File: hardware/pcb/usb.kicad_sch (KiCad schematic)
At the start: 6 parts, among them J3 USB_C_Receptacle_USB2.0_16P, U5 ECMF02-2AMX6

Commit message: started cleaning up schematic
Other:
- company: (none) -> Gensis
- title: (none) -> USB
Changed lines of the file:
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@@
 	(generator_version "10.0")
 	(paper "A5")
+	(title_block
+		(title "USB")
+		(rev "v1.0.0")
+		(company "Gensis")
+	)
 	(rectangle
 		(start 138.43 33.02)

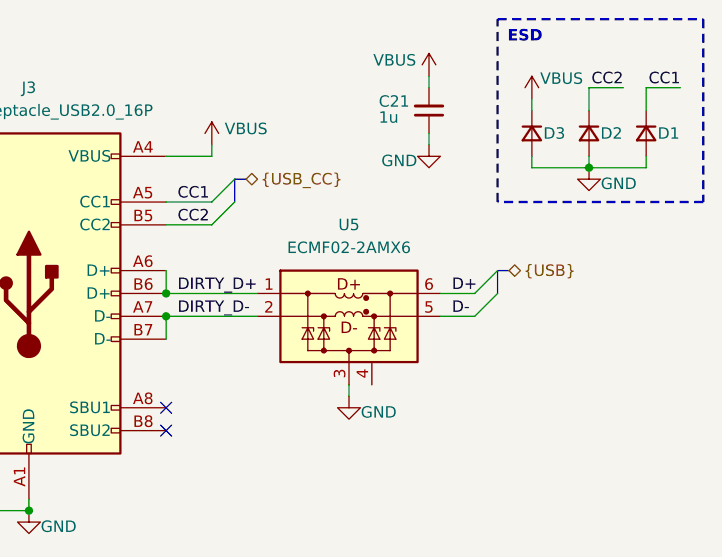
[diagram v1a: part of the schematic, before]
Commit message: main board: fixed schematic errors, made sama7 symbol better
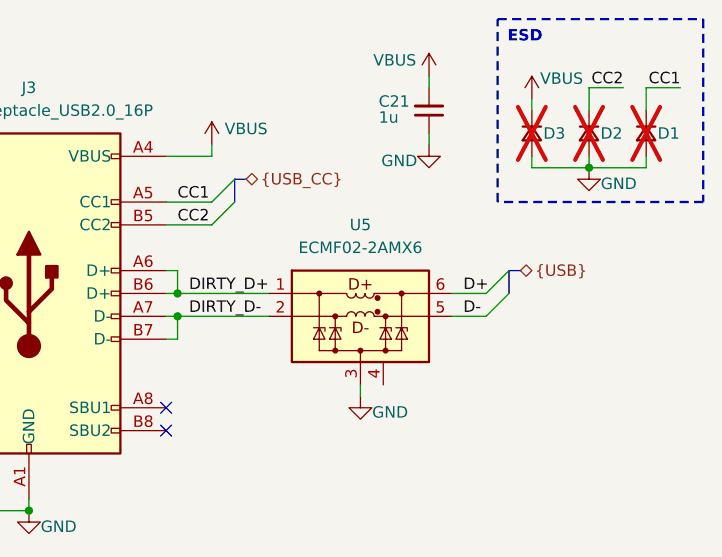
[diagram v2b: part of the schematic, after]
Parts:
- D1, D2, D3: now not fitted; now left out of the parts list
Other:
- moved on the sheet: U5
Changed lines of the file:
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@@
 	)
 	(junction
-		(at 101.6 66.04)
+		(at 102.87 66.04)
 		(diameter 0)
 		(color 0 0 0 0)
@@
 	)
 	(junction
-		(at 101.6 63.5)
+		(at 102.87 63.5)
 		(diameter 0)
 		(color 0 0 0 0)
@@
 	)
 	(bus_entry
-		(at 138.43 63.5)
+		(at 139.7 63.5)
 		(size -2.54 2.54)
 		(stroke
@@
 	)
 	(bus_entry
-		(at 138.43 60.96)
+		(at 139.7 60.96)
 		(size -2.54 2.54)
 		(stroke
@@
 	(wire
 		(pts
-			(xy 121.92 73.66) (xy 121.92 74.93)
-		)
-		(stroke
-			(width 0)
-			(type default)
-		)
-	)
-	(wire
-		(pts
-			(xy 101.6 66.04) (xy 111.76 66.04)
+			(xy 123.19 73.66) (xy 123.19 74.93)
 		)
 		(stroke
@@
 	(wire
 		(pts
+			(xy 102.87 60.96) (xy 101.6 60.96)
+		)
+		(stroke
+			(width 0)
+			(type default)
+		)
+	)
+	(wire
+		(pts
 			(xy 154.94 40.64) (xy 158.75 40.64)
 		)
@@
 	(wire
 		(pts
+			(xy 102.87 63.5) (xy 101.6 63.5)
+		)
+		(stroke
+			(width 0)
+			(type default)
+		)
+	)
+	(wire
+		(pts
 			(xy 142.24 48.26) (xy 142.24 49.53)
 		)
@@
 		)
 	)
+	(wire
+		(pts
+			(xy 102.87 66.04) (xy 113.03 66.04)
+		)
+		(stroke
+			(width 0)
+			(type default)
+		)
+	)
 	(bus
 		(pts
-			(xy 138.43 60.96) (xy 138.43 63.5)
+			(xy 139.7 60.96) (xy 139.7 63.5)
 		)
 		(stroke
@@
 	(wire
 		(pts
+			(xy 102.87 66.04) (xy 101.6 66.04)
+		)
+		(stroke
+			(width 0)
+			(type default)
+		)
+	)
+	(wire
+		(pts
+			(xy 102.87 68.58) (xy 101.6 68.58)
+		)
+		(stroke
+			(width 0)
+			(type default)
+		)
+	)
+	(wire
+		(pts
 			(xy 148.59 48.26) (xy 148.59 49.53)
 		)
@@
 	(wire
 		(pts
-			(xy 132.08 66.04) (xy 135.89 66.04)
+			(xy 133.35 66.04) (xy 137.16 66.04)
 		)
 		(stroke
@@
 	(wire
 		(pts
-			(xy 132.08 63.5) (xy 135.89 63.5)
+			(xy 133.35 63.5) (xy 137.16 63.5)
 		)
 		(stroke
@@
 	(wire
 		(pts
-			(xy 101.6 63.5) (xy 111.76 63.5)
-		)
-		(stroke
-			(width 0)
-			(type default)
-		)
-	)
-	(wire
-		(pts
 			(xy 101.6 55.88) (xy 106.68 55.88)
 		)
@@
 	(wire
 		(pts
-			(xy 101.6 66.04) (xy 101.6 68.58)
+			(xy 102.87 66.04) (xy 102.87 68.58)
+		)
+		(stroke
+			(width 0)
+			(type default)
+		)
+	)
+	(wire
+		(pts
+			(xy 102.87 63.5) (xy 113.03 63.5)
 		)
 		(stroke
@@
 	(bus
 		(pts
-			(xy 139.7 60.96) (xy 138.43 60.96)
-		)
-		(stroke
-			(width 0)
-			(type default)
-		)
-	)
-	(wire
-		(pts
-			(xy 101.6 60.96) (xy 101.6 63.5)
+			(xy 140.97 60.96) (xy 139.7 60.96)
+		)
+		(stroke
+			(width 0)
+			(type default)
+		)
+	)
+	(wire
+		(pts
+			(xy 102.87 60.96) (xy 102.87 63.5)
 		)
 		(stroke
@@
 	)
 	(label "DIRTY_D+"
-		(at 102.87 63.5 0)
+		(at 104.14 63.5 0)
 		(effects
 			(font
@@
 	)
 	(label "DIRTY_D-"
-		(at 102.87 66.04 0)
+		(at 104.14 66.04 0)
 		(effects
 			(font
@@
 	)
 	(label "D+"
-		(at 133.35 63.5 0)
+		(at 134.62 63.5 0)
 		(effects
 			(font
@@
 	)
 	(label "D-"
-		(at 133.35 66.04 0)
+		(at 134.62 66.04 0)
 		(effects
 			(font
@@
 	(hierarchical_label "{USB}"
 		(shape bidirectional)
-		(at 139.7 60.96 0)
+		(at 140.97 60.96 0)
 		(effects
 			(font
@@
 		(body_style 1)
 		(exclude_from_sim no)
-		(in_bom yes)
-		(on_board yes)
-		(in_pos_files yes)
-		(dnp no)
+		(in_bom no)
+		(on_board no)
+		(in_pos_files no)
+		(dnp yes)
 		(property "Reference" "D1"
 			(at 156.21 45.72 90)
@@
 	(symbol
 		(lib_id "Power_Protection:ECMF02-2AMX6")
-		(at 121.92 66.04 0)
+		(at 123.19 66.04 0)
 		(unit 1)
 		(body_style 1)
@@
 		(fields_autoplaced yes)
 		(property "Reference" "U5"
-			(at 121.92 55.88 0)
+			(at 123.19 55.88 0)
 			(show_name no)
 			(do_not_autoplace no)
@@
 		)
 		(property "Value" "ECMF02-2AMX6"
-			(at 121.92 58.42 0)
+			(at 123.19 58.42 0)
 			(show_name no)
 			(do_not_autoplace no)
@@
 		)
 		(property "Footprint" "Package_DFN_QFN:ST_UQFN-6L_1.5x1.7mm_P0.5mm"
-			(at 121.92 86.36 0)
+			(at 123.19 86.36 0)
 			(hide yes)
 			(show_name no)
@@
 		)
 		(property "Datasheet" "https://www.st.com/resource/en/datasheet/ecmf02-2amx6.pdf"
-			(at 121.92 88.9 0)
+			(at 123.19 88.9 0)
 			(hide yes)
 			(show_name no)
@@
 		)
 		(property "Description" "Single Pair Common Mode Filter with ESD Protection, UQFN-6L"
-			(at 121.92 66.04 0)
+			(at 123.19 66.04 0)
 			(hide yes)
 			(show_name no)
@@
 		)
 		(property "KLC_S3.3" ""
-			(at 121.92 66.04 0)
+			(at 123.19 66.04 0)
 			(hide yes)
 			(show_name no)
@@
 		)
 		(property "KLC_S4.1" ""
-			(at 121.92 66.04 0)
+			(at 123.19 66.04 0)
 			(hide yes)
 			(show_name no)
@@
 	(symbol
 		(lib_id "power:GND")
-		(at 121.92 74.93 0)
+		(at 123.19 74.93 0)
 		(unit 1)
 		(body_style 1)
@@
 		(dnp no)
 		(property "Reference" "#PWR013"
-			(at 121.92 81.28 0)
+			(at 123.19 81.28 0)
 			(hide yes)
 			(show_name no)
@@
 		)
 		(property "Value" "GND"
-			(at 125.222 76.708 0)
+			(at 126.492 76.708 0)
 			(show_name no)
 			(do_not_autoplace no)
@@
 		)
 		(property "Footprint" ""
-			(at 121.92 74.93 0)
+			(at 123.19 74.93 0)
 			(hide yes)
 			(show_name no)
@@
 		)
 		(property "Datasheet" ""
-			(at 121.92 74.93 0)
+			(at 123.19 74.93 0)
 			(hide yes)
 			(show_name no)
@@
 		)
 		(property "Description" "Power symbol creates a global label with name \"GND\" , ground"
-			(at 121.92 74.93 0)
+			(at 123.19 74.93 0)
 			(hide yes)
 			(show_name no)
@@
 		(body_style 1)
 		(exclude_from_sim no)
-		(in_bom yes)
-		(on_board yes)
-		(in_pos_files yes)
-		(dnp no)
+		(in_bom no)
+		(on_board no)
+		(in_pos_files no)
+		(dnp yes)
 		(property "Reference" "D3"
 			(at 143.51 45.72 90)
@@
 		(body_style 1)
 		(exclude_from_sim no)
-		(in_bom yes)
-		(on_board yes)
-		(in_pos_files yes)
-		(dnp no)
+		(in_bom no)
+		(on_board no)
+		(in_pos_files no)
+		(dnp yes)
 		(property "Reference" "D2"
 			(at 149.86 45.72 90)

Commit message: mainboard: adde notes
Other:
- note added: "No ESD protection added for these nets For first protype this is fine Will be added later"
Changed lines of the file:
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@@
+		)
+	)
+	(text "No ESD protection added for these nets\nFor first protype this is fine\nWill be added later"
+		(exclude_from_sim no)
+		(at 138.684 32.512 0)
+		(effects
+			(font
+				(size 1.27 1.27)
+				(thickness 0.1588)
+			)
+			(justify left bottom)
 		)
 	)

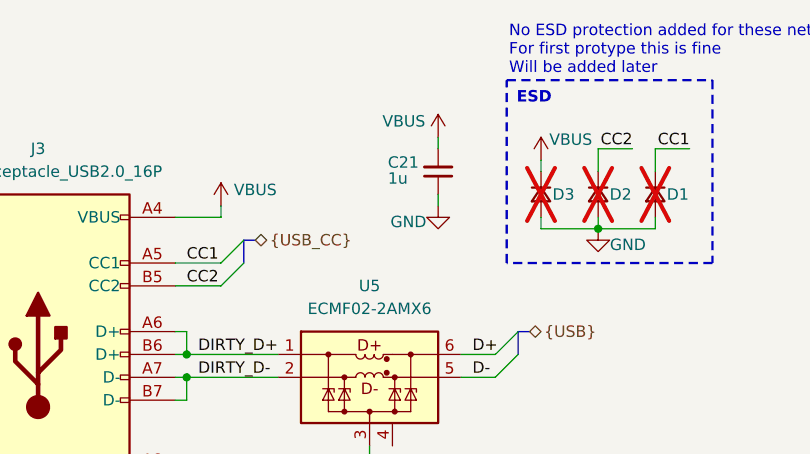
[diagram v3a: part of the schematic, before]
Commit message: mainboard: finished touchpad schematic
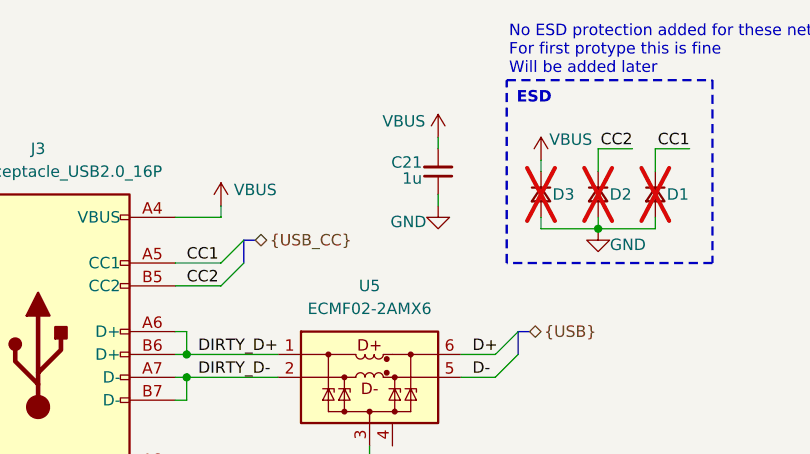
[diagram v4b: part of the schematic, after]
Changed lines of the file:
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@@
 		(dnp no)
 		(property "Reference" "C21"
-			(at 125.222 42.164 0)
+			(at 129.032 42.164 0)
 			(show_name no)
 			(do_not_autoplace no)
@@
 					(size 1.27 1.27)
 				)
-				(justify left)
+				(justify right)
 			)
 		)
 		(property "Value" "1u"
-			(at 125.222 43.942 0)
+			(at 129.032 43.942 0)
 			(show_name no)
 			(do_not_autoplace no)
@@
 					(size 1.27 1.27)
 				)
-				(justify left)
+				(justify right)
 			)
 		)

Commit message: mainboard: reannotated schematic
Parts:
- renumbered C21 to C110, D3 to D2, D2 to D3, D1 to D4, U5 to U6
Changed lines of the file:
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@@
 		(in_pos_files yes)
 		(dnp no)
-		(property "Reference" "#PWR012"
+		(property "Reference" "#PWR0102"
 			(at 86.36 93.98 0)
 			(hide yes)
@@
 			(project "meko"
 				(path "/da54f10a-146b-4941-a9c7-55c7173bb101/13ed9585-0f16-442f-add9-c716aca8a0ac"
-					(reference "#PWR012")
+					(reference "#PWR0102")
 					(unit 1)
 				)
@@
 		(in_pos_files no)
 		(dnp yes)
-		(property "Reference" "D1"
+		(property "Reference" "D4"
 			(at 156.21 45.72 90)
 			(show_name no)
@@
 			(project "meko"
 				(path "/da54f10a-146b-4941-a9c7-55c7173bb101/13ed9585-0f16-442f-add9-c716aca8a0ac"
-					(reference "D1")
+					(reference "D4")
 					(unit 1)
 				)
@@
 		(dnp no)
 		(fields_autoplaced yes)
-		(property "Reference" "U5"
+		(property "Reference" "U6"
 			(at 123.19 55.88 0)
 			(show_name no)
@@
 			(project "meko"
 				(path "/da54f10a-146b-4941-a9c7-55c7173bb101/13ed9585-0f16-442f-add9-c716aca8a0ac"
-					(reference "U5")
+					(reference "U6")
 					(unit 1)
 				)
@@
 		(in_pos_files yes)
 		(dnp no)
-		(property "Reference" "#PWR013"
+		(property "Reference" "#PWR0101"
 			(at 123.19 81.28 0)
 			(hide yes)
@@
 			(project "meko"
 				(path "/da54f10a-146b-4941-a9c7-55c7173bb101/13ed9585-0f16-442f-add9-c716aca8a0ac"
-					(reference "#PWR013")
+					(reference "#PWR0101")
 					(unit 1)
 				)
@@
 		(in_pos_files yes)
 		(dnp no)
-		(property "Reference" "#PWR019"
+		(property "Reference" "#PWR099"
 			(at 130.81 53.34 0)
 			(hide yes)
@@
 			(project "meko"
 				(path "/da54f10a-146b-4941-a9c7-55c7173bb101/13ed9585-0f16-442f-add9-c716aca8a0ac"
-					(reference "#PWR019")
+					(reference "#PWR099")
 					(unit 1)
 				)
@@
 		(in_pos_files yes)
 		(dnp no)
-		(property "Reference" "#PWR015"
+		(property "Reference" "#PWR097"
 			(at 142.24 45.72 0)
 			(hide yes)
@@
 			(project "meko"
 				(path "/da54f10a-146b-4941-a9c7-55c7173bb101/13ed9585-0f16-442f-add9-c716aca8a0ac"
-					(reference "#PWR015")
+					(reference "#PWR097")
 					(unit 1)
 				)
@@
 		(in_pos_files yes)
 		(dnp no)
-		(property "Reference" "#PWR016"
+		(property "Reference" "#PWR0100"
 			(at 148.59 55.88 0)
 			(hide yes)
@@
 			(project "meko"
 				(path "/da54f10a-146b-4941-a9c7-55c7173bb101/13ed9585-0f16-442f-add9-c716aca8a0ac"
-					(reference "#PWR016")
+					(reference "#PWR0100")
 					(unit 1)
 				)
@@
 		(in_pos_files yes)
 		(dnp no)
-		(property "Reference" "#PWR014"
+		(property "Reference" "#PWR098"
 			(at 106.68 50.8 0)
 			(hide yes)
@@
 			(project "meko"
 				(path "/da54f10a-146b-4941-a9c7-55c7173bb101/13ed9585-0f16-442f-add9-c716aca8a0ac"
-					(reference "#PWR014")
+					(reference "#PWR098")
 					(unit 1)
 				)
@@
 		(in_pos_files yes)
 		(dnp no)
-		(property "Reference" "C21"
+		(property "Reference" "C110"
 			(at 129.032 42.164 0)
 			(show_name no)
@@
 			(project "meko"
 				(path "/da54f10a-146b-4941-a9c7-55c7173bb101/13ed9585-0f16-442f-add9-c716aca8a0ac"
-					(reference "C21")
+					(reference "C110")
 					(unit 1)
 				)
@@
 		(in_pos_files no)
 		(dnp yes)
-		(property "Reference" "D3"
+		(property "Reference" "D2"
 			(at 143.51 45.72 90)
 			(show_name no)
@@
 			(project "meko"
 				(path "/da54f10a-146b-4941-a9c7-55c7173bb101/13ed9585-0f16-442f-add9-c716aca8a0ac"
-					(reference "D3")
+					(reference "D2")
 					(unit 1)
 				)
@@
 		(in_pos_files no)
 		(dnp yes)
-		(property "Reference" "D2"
+		(property "Reference" "D3"
 			(at 149.86 45.72 90)
 			(show_name no)
@@
 			(project "meko"
 				(path "/da54f10a-146b-4941-a9c7-55c7173bb101/13ed9585-0f16-442f-add9-c716aca8a0ac"
-					(reference "D2")
+					(reference "D3")
 					(unit 1)
 				)
@@
 		(in_pos_files yes)
 		(dnp no)
-		(property "Reference" "#PWR018"
+		(property "Reference" "#PWR096"
 			(at 130.81 43.18 0)
 			(hide yes)
@@
 			(project "meko"
 				(path "/da54f10a-146b-4941-a9c7-55c7173bb101/13ed9585-0f16-442f-add9-c716aca8a0ac"
-					(reference "#PWR018")
+					(reference "#PWR096")
 					(unit 1)
 				)

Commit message: added a bunch testpoints
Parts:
- added TP20: CC1, TestPoint:TestPoint_Pad_D1.0mm, symbol Connector:TestPoint
- added TP21: CC2, TestPoint:TestPoint_Pad_D1.0mm, symbol Connector:TestPoint
- added TP51: VBUS, TestPoint:TestPoint_Pad_D1.0mm, symbol Connector:TestPoint
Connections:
- net CC1: now also TP20.1
- net CC2: now also TP21.1
- net VBUS: now also TP51.1
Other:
- moved on the sheet: C110, D2, D3, D4, J3, U6

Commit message: removed testpoints on sd cards, since I can probe the pins there
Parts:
- renumbered TP51 to TP47, TP20 to TP48, TP21 to TP49
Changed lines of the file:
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@@
 		(in_pos_files yes)
 		(dnp no)
-		(property "Reference" "#PWR0102"
+		(property "Reference" "#PWR096"
 			(at 36.83 93.98 0)
 			(hide yes)
@@
 			(project "meko"
 				(path "/da54f10a-146b-4941-a9c7-55c7173bb101/13ed9585-0f16-442f-add9-c716aca8a0ac"
-					(reference "#PWR0102")
+					(reference "#PWR096")
 					(unit 1)
 				)
@@
 		(in_pos_files yes)
 		(dnp no)
-		(property "Reference" "TP21"
+		(property "Reference" "TP49"
 			(at 141.224 81.026 90)
 			(show_name no)
@@
 			(project "meko"
 				(path "/da54f10a-146b-4941-a9c7-55c7173bb101/13ed9585-0f16-442f-add9-c716aca8a0ac"
-					(reference "TP21")
+					(reference "TP49")
 					(unit 1)
 				)
@@
 		(in_pos_files yes)
 		(dnp no)
-		(property "Reference" "TP51"
+		(property "Reference" "TP47"
 			(at 54.61 33.782 0)
 			(show_name no)
@@
 			(project "meko"
 				(path "/da54f10a-146b-4941-a9c7-55c7173bb101/13ed9585-0f16-442f-add9-c716aca8a0ac"
-					(reference "TP51")
+					(reference "TP47")
 					(unit 1)
 				)
@@
 		(in_pos_files yes)
 		(dnp no)
-		(property "Reference" "#PWR0101"
+		(property "Reference" "#PWR098"
 			(at 73.66 81.28 0)
 			(hide yes)
@@
 			(project "meko"
 				(path "/da54f10a-146b-4941-a9c7-55c7173bb101/13ed9585-0f16-442f-add9-c716aca8a0ac"
-					(reference "#PWR0101")
+					(reference "#PWR098")
 					(unit 1)
 				)
@@
 		(in_pos_files yes)
 		(dnp no)
-		(property "Reference" "#PWR099"
+		(property "Reference" "#PWR0100"
 			(at 81.28 53.34 0)
 			(hide yes)
@@
 			(project "meko"
 				(path "/da54f10a-146b-4941-a9c7-55c7173bb101/13ed9585-0f16-442f-add9-c716aca8a0ac"
-					(reference "#PWR099")
+					(reference "#PWR0100")
 					(unit 1)
 				)
@@
 		(in_pos_files yes)
 		(dnp no)
-		(property "Reference" "#PWR097"
+		(property "Reference" "#PWR0101"
 			(at 92.71 45.72 0)
 			(hide yes)
@@
 			(project "meko"
 				(path "/da54f10a-146b-4941-a9c7-55c7173bb101/13ed9585-0f16-442f-add9-c716aca8a0ac"
-					(reference "#PWR097")
+					(reference "#PWR0101")
 					(unit 1)
 				)
@@
 		(in_pos_files yes)
 		(dnp no)
-		(property "Reference" "#PWR0100"
+		(property "Reference" "#PWR0102"
 			(at 99.06 55.88 0)
 			(hide yes)
@@
 			(project "meko"
 				(path "/da54f10a-146b-4941-a9c7-55c7173bb101/13ed9585-0f16-442f-add9-c716aca8a0ac"
-					(reference "#PWR0100")
+					(reference "#PWR0102")
 					(unit 1)
 				)
@@
 		(in_pos_files yes)
 		(dnp no)
-		(property "Reference" "#PWR098"
+		(property "Reference" "#PWR097"
 			(at 57.15 50.8 0)
 			(hide yes)
@@
 			(project "meko"
 				(path "/da54f10a-146b-4941-a9c7-55c7173bb101/13ed9585-0f16-442f-add9-c716aca8a0ac"
-					(reference "#PWR098")
+					(reference "#PWR097")
 					(unit 1)
 				)
@@
 		(in_pos_files yes)
 		(dnp no)
-		(property "Reference" "TP20"
+		(property "Reference" "TP48"
 			(at 141.224 78.486 90)
 			(show_name no)
@@
 			(project "meko"
 				(path "/da54f10a-146b-4941-a9c7-55c7173bb101/13ed9585-0f16-442f-add9-c716aca8a0ac"
-					(reference "TP20")
+					(reference "TP48")
 					(unit 1)
 				)
@@
 		(in_pos_files yes)
 		(dnp no)
-		(property "Reference" "#PWR096"
+		(property "Reference" "#PWR099"
 			(at 81.28 43.18 0)
 			(hide yes)
@@
 			(project "meko"
 				(path "/da54f10a-146b-4941-a9c7-55c7173bb101/13ed9585-0f16-442f-add9-c716aca8a0ac"
-					(reference "#PWR096")
-					(unit 1)
-				)
+					(reference "#PWR099")
+					(unit 1)
+				)

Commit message: added capacitor to sama ddr vref pin
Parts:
- renumbered C110 to C112
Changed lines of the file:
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@@
 		(in_pos_files yes)
 		(dnp no)
-		(property "Reference" "#PWR096"
+		(property "Reference" "#PWR098"
 			(at 36.83 93.98 0)
 			(hide yes)
@@
 			(project "meko"
 				(path "/da54f10a-146b-4941-a9c7-55c7173bb101/13ed9585-0f16-442f-add9-c716aca8a0ac"
-					(reference "#PWR096")
+					(reference "#PWR098")
 					(unit 1)
 				)
@@
 		(in_pos_files yes)
 		(dnp no)
-		(property "Reference" "#PWR098"
+		(property "Reference" "#PWR0100"
 			(at 73.66 81.28 0)
 			(hide yes)
@@
 			(project "meko"
 				(path "/da54f10a-146b-4941-a9c7-55c7173bb101/13ed9585-0f16-442f-add9-c716aca8a0ac"
-					(reference "#PWR098")
+					(reference "#PWR0100")
 					(unit 1)
 				)
@@
 		(in_pos_files yes)
 		(dnp no)
-		(property "Reference" "#PWR0100"
+		(property "Reference" "#PWR0102"
 			(at 81.28 53.34 0)
 			(hide yes)
@@
 			(project "meko"
 				(path "/da54f10a-146b-4941-a9c7-55c7173bb101/13ed9585-0f16-442f-add9-c716aca8a0ac"
-					(reference "#PWR0100")
+					(reference "#PWR0102")
 					(unit 1)
 				)
@@
 		(in_pos_files yes)
 		(dnp no)
-		(property "Reference" "#PWR0101"
+		(property "Reference" "#PWR0103"
 			(at 92.71 45.72 0)
 			(hide yes)
@@
 			(project "meko"
 				(path "/da54f10a-146b-4941-a9c7-55c7173bb101/13ed9585-0f16-442f-add9-c716aca8a0ac"
-					(reference "#PWR0101")
+					(reference "#PWR0103")
 					(unit 1)
 				)
@@
 		(in_pos_files yes)
 		(dnp no)
-		(property "Reference" "#PWR0102"
+		(property "Reference" "#PWR0104"
 			(at 99.06 55.88 0)
 			(hide yes)
@@
 			(project "meko"
 				(path "/da54f10a-146b-4941-a9c7-55c7173bb101/13ed9585-0f16-442f-add9-c716aca8a0ac"
-					(reference "#PWR0102")
+					(reference "#PWR0104")
 					(unit 1)
 				)
@@
 		(in_pos_files yes)
 		(dnp no)
-		(property "Reference" "#PWR097"
+		(property "Reference" "#PWR099"
 			(at 57.15 50.8 0)
 			(hide yes)
@@
 			(project "meko"
 				(path "/da54f10a-146b-4941-a9c7-55c7173bb101/13ed9585-0f16-442f-add9-c716aca8a0ac"
-					(reference "#PWR097")
+					(reference "#PWR099")
 					(unit 1)
 				)
@@
 		(in_pos_files yes)
 		(dnp no)
-		(property "Reference" "C110"
+		(property "Reference" "C112"
 			(at 79.502 42.164 0)
 			(show_name no)
@@
 			(project "meko"
 				(path "/da54f10a-146b-4941-a9c7-55c7173bb101/13ed9585-0f16-442f-add9-c716aca8a0ac"
-					(reference "C110")
+					(reference "C112")
 					(unit 1)
 				)
@@
 		(in_pos_files yes)
 		(dnp no)
-		(property "Reference" "#PWR099"
+		(property "Reference" "#PWR0101"
 			(at 81.28 43.18 0)
 			(hide yes)
@@
 			(project "meko"
 				(path "/da54f10a-146b-4941-a9c7-55c7173bb101/13ed9585-0f16-442f-add9-c716aca8a0ac"
-					(reference "#PWR099")
-					(unit 1)
-				)
+					(reference "#PWR0101")
+					(unit 1)
+				)
